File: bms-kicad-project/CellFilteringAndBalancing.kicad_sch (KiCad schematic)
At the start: 41 parts

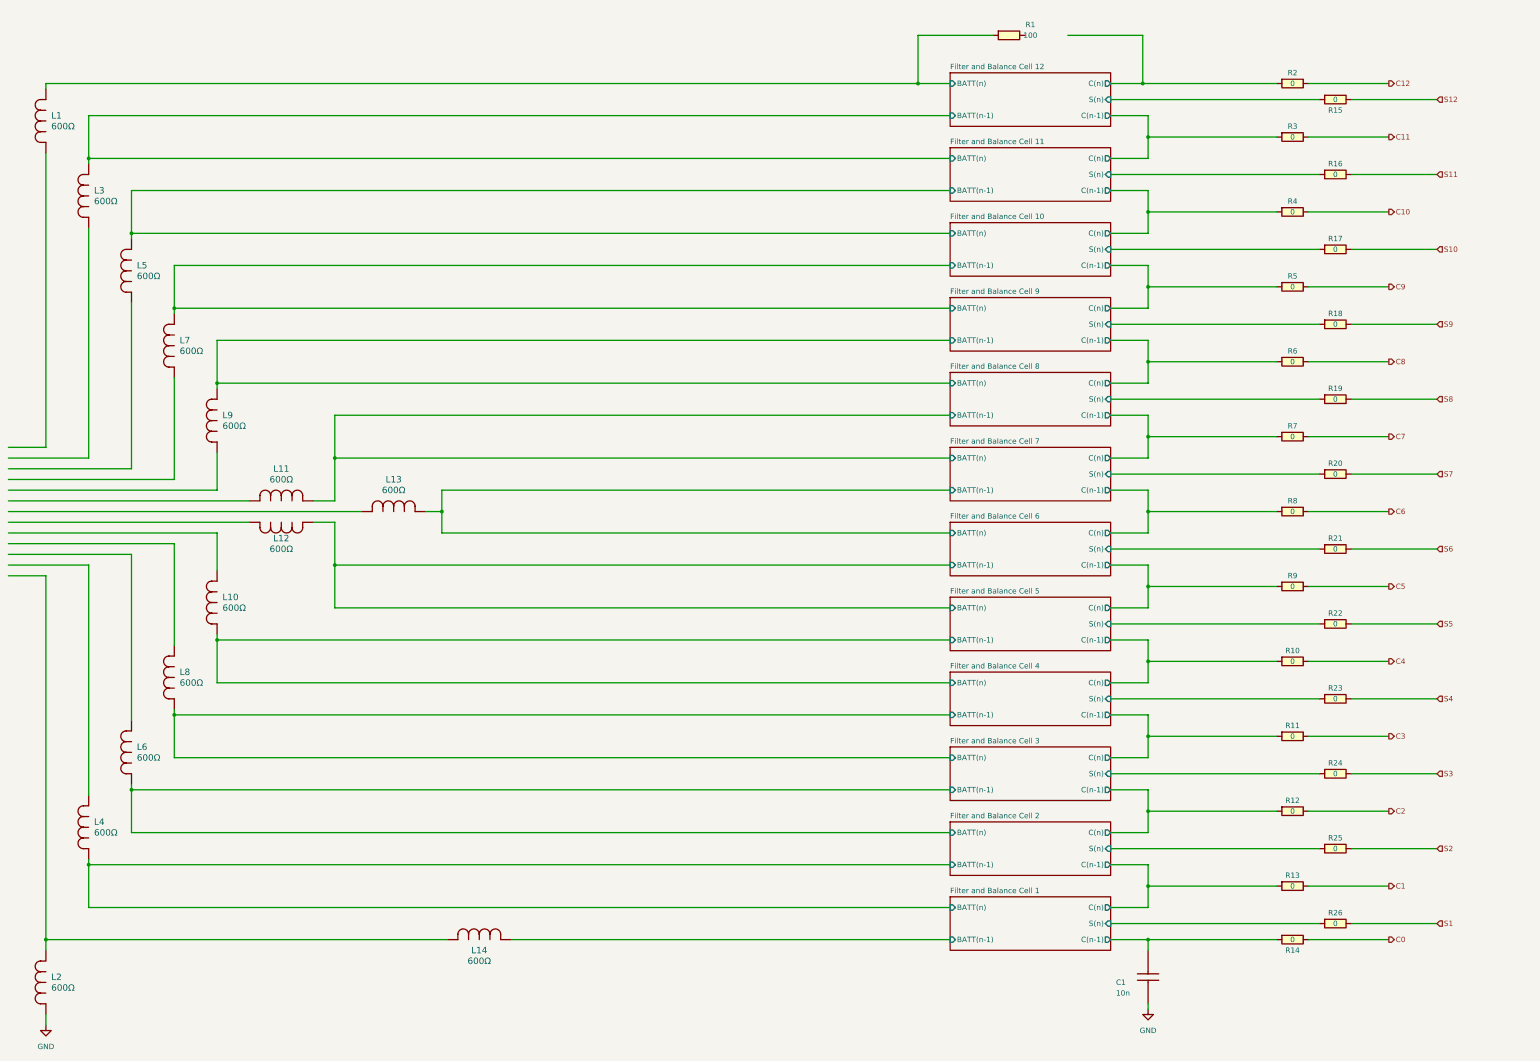
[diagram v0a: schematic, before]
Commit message: Feature/current sensor (#17)
* feat: making sure my git still works

* feat: figured out battery stack monitor V+ biasing. Refer to task 5 on the punchlist for more details.

* feat: swapped out battery<->18V diode for cheaper alternative

* feat: started a new sheet for external connections and added current sensor

* feat: made a placeholder label to connect current sensor to LTC6811 GPIO

* feat: added remaining connectors to component library

* Wired up most external connections

* feat: Just shifting a few things around
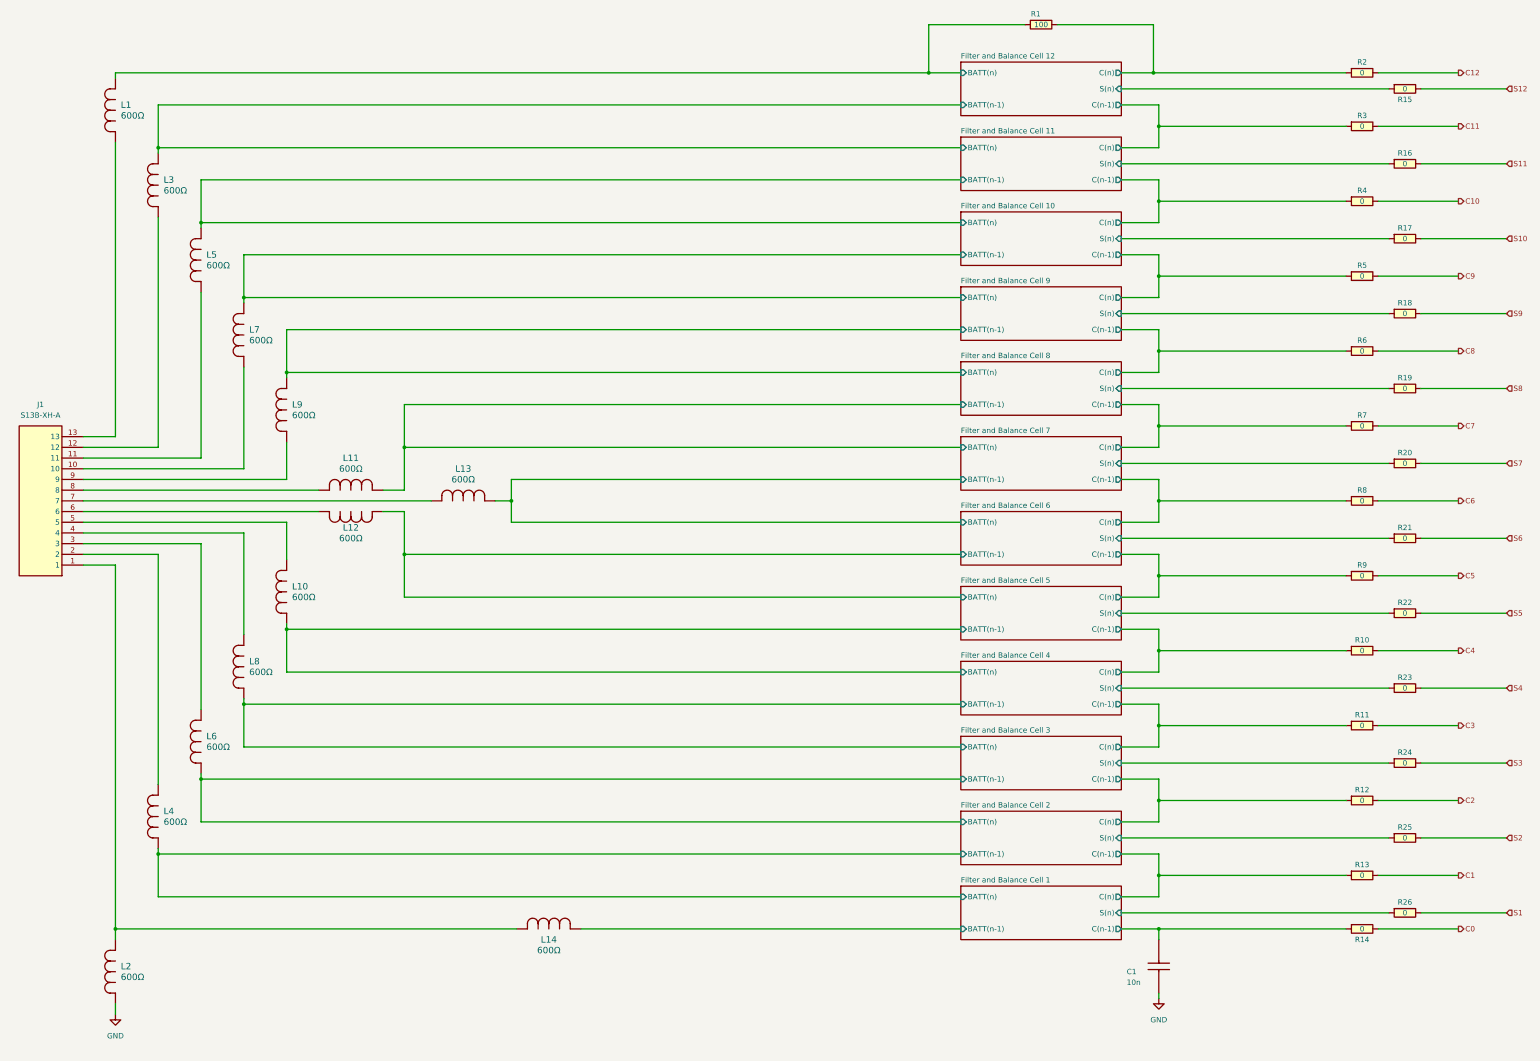
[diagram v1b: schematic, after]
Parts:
- added J1: S13B-XH-A, FixedWing:S13BXHALFSN, symbol FixedWing:S13B-XH-A
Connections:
- net Filter and Balance Cell 12/C(n): now also R1.2
- net at L7.2: now also J1.10
- net at L11.2: now also J1.8
- net at L14.2, L2.1: now also J1.1
- net at L9.2: now also J1.9
- net at L12.1: now also J1.6
- net at L13.2: now also J1.7
- net at L8.1: now also J1.4
- net at L6.1: now also J1.3
- net at L3.2: now also J1.12
- net at L1.2: now also J1.13
- net at L5.2: now also J1.11
- net at L4.1: now also J1.2
- net at L10.1: now also J1.5
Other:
- moved on the sheet: C1, L1, L10, L11, L12, L13, L14, L2, L3, L4, L5, L6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

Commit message: feat: added sims directory, new cell balancing components
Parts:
- C1: Manufacturer Name (none) -> YAGEO; Manufacturer Part Number (none) -> AC0805KRX7R8BB103
- R1: Manufacturer (none) -> Vishay; Manufacturer Part Number (none) -> CRCW0805100RFKEA
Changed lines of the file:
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@@
+      (effects (font (size 1.27 1.27)) (justify left top) hide)
+    )
+    (property "Manufacturer Name" "YAGEO" (at -401.55 245.11 0)
+      (effects (font (size 1.27 1.27)) (justify left top) hide)
+    )
+    (property "Manufacturer Part Number" "AC0805KRX7R8BB103" (at -501.55 245.11 0)
       (effects (font (size 1.27 1.27)) (justify left top) hide)
     )
@@
       (effects (font (size 1.27 1.27)) (justify left top) hide)
     )
+    (property "Manufacturer" "Vishay" (at 276.86 715.24 0)
+      (effects (font (size 1.27 1.27)) (justify left top) hide)
+    )
+    (property "Manufacturer Part Number" "CRCW0805100RFKEA" (at 276.86 815.24 0)
+      (effects (font (size 1.27 1.27)) (justify left top) hide)
+    )
